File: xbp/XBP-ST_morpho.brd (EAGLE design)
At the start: 68.9 x 31.1 mm, 4 parts

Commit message: XBX ST morpho Adapter version 1.0
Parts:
- removed JP6: VCCDin, pinhead:1X01
- added JP1: (no value), pinhead:2X10
- JP3: value (none) -> VCCDin; device pinhead:2X10 -> pinhead:1X01
- moved JP3 14.4 mm to (14.0, 5.08), turned to 0 degrees
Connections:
- net GND: now also JP1.19, JP1.20, JP1.8, JP4.20; no longer JP3.8
- net N$6: now also JP1.16, JP2.4, JP3.1; no longer JP3.16, JP6.1
- net RSTD: now also JP1.14; no longer JP3.14
- net VCCD: now also JP1.5; no longer JP3.5
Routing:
- net N$6: track 13.5 -> 34.0 mm
- net TF0D: track 43.3 -> 34.3 mm, vias 0 -> 1
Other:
- board text added: "Align with Top of ST Morpho Connector (pins 1 and 2)"
- board text added: "JP1"
- board text added: "JP3"
- board text added: "JP4"
- board text added: "VCCDin"
- board text added: "VIN"
- board text added: "XXBX: XBP - ST morpho Adapter"
- board text added: "rev 1.0"
- board text removed: "+"
- board text removed: "0"
- board text removed: "0b"
- board text removed: "1"
- board text removed: "10"
- board text removed: "100"
- board text removed: "11"
- board text removed: "1a"
- board text removed: "1b"
- board text removed: "2"
- board text removed: "20"
- board text removed: "200"
- board text removed: "21"
- board text removed: "25"
- board text removed: "2a"
- board text removed: "2b"
- board text removed: "3"
- board text removed: "30"
- board text removed: "31"
- board text removed: "3a"
- board text removed: "3b"
- board text removed: "40"
- board text removed: "50"
- board text removed: "5V"
- board text removed: "Activity"
- board text removed: "C1"
- board text removed: "C2"
- board text removed: "C3"
- board text removed: "GS0a"
- board text removed: "GS1a"
- board text removed: "GS2a"
- board text removed: "GS3a"
- board text removed: "GS3b"
- board text removed: "Gain"
- board text removed: "IC1"
- board text removed: "J1"
- board text removed: "J2"
- board text removed: "J3"
- board text removed: "J4"
- board text removed: "JP5"
- board text removed: "PWR3"
- board text removed: "Power"
- board text removed: "Q1"
- board text removed: "Q2"
- board text removed: "Q3"
- board text removed: "Q4"
- board text removed: "Q5"
- board text removed: "Q6"
- board text removed: "Q7"
- board text removed: "Q8"
- board text removed: "R1"
- board text removed: "R10"
- board text removed: "R11"
- board text removed: "R12"
- board text removed: "R13"
- board text removed: "R2"
- board text removed: "R3"
- board text removed: "R4"
- board text removed: "R5"
- board text removed: "R6"
- board text removed: "R7"
- board text removed: "R8"
- board text removed: "R9"
- board text removed: "RST0"
- board text removed: "RST1"
- board text removed: "SJ1"
- board text removed: "SJ2"
- board text removed: "SJ3"
- board text removed: "SJ4"
- board text removed: "SJ5"
- board text removed: "TF0"
- board text removed: "TF1"
- board text removed: "TF2"
- board text removed: "TF3"
- board text removed: "U1"
- board text removed: "VccD"
- board text removed: "VccH"
- board text removed: "VccP"
- board text removed: "X1"
- board text removed: "XBH"
- board text removed: "XBP"
- board text removed: "rev 2.0"

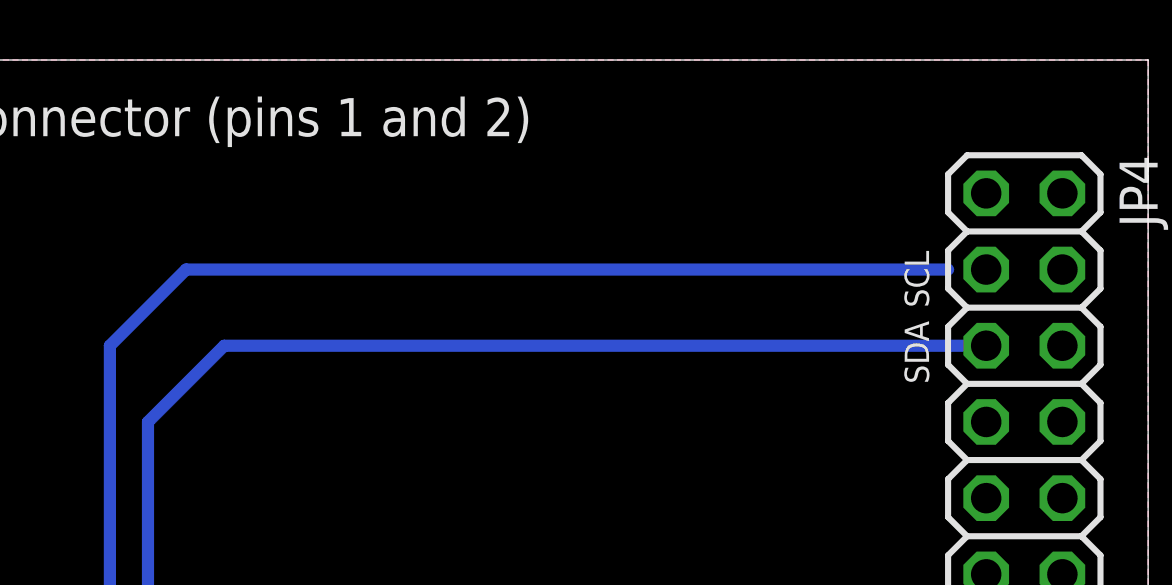
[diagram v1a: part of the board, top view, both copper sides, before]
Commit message: SCL was not connected to ST Morpho Pin
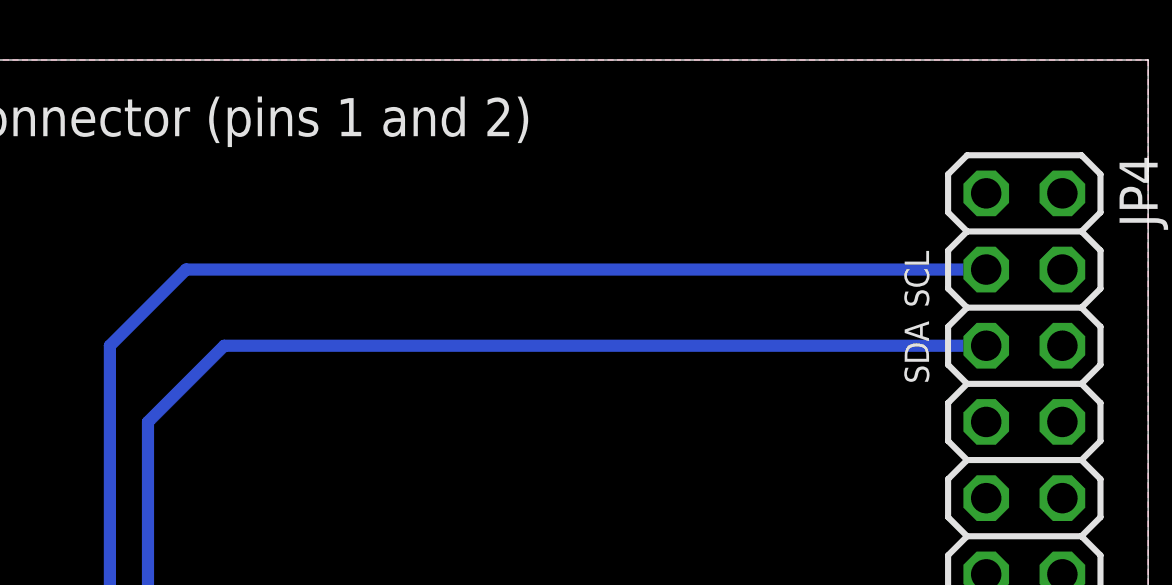
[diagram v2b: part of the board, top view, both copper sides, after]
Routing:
- net SCLD: track 46.0 -> 47.3 mm
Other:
- board text added: "rev 1.1"
- board text removed: "rev 1.0"
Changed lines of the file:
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@@
 <text x="34.29" y="24.13" size="1.27" layer="122" font="vector" ratio="16" rot="MR0" align="bottom-center">cryptography.gmu.edu</text>
 <text x="34.29" y="21.59" size="1.27" layer="122" font="vector" ratio="16" rot="MR0" align="bottom-center">XXBX: XBP - ST morpho Adapter</text>
-<text x="34.29" y="19.05" size="1.27" layer="122" font="vector" ratio="16" rot="MR0" align="bottom-center">rev 1.0</text>
+<text x="34.29" y="19.05" size="1.27" layer="122" font="vector" ratio="16" rot="MR0" align="bottom-center">rev 1.1</text>
 <text x="6.35" y="28.575" size="1.27" layer="121" font="vector" ratio="16">Align with Top of ST Morpho Connector (pins 1 and 2)</text>
 </plain>
@@
 <wire x1="34.29" y1="6.35" x2="34.29" y2="21.59" width="0.4064" layer="16"/>
 <wire x1="34.29" y1="21.59" x2="36.83" y2="24.13" width="0.4064" layer="16"/>
-<wire x1="36.83" y1="24.13" x2="62.23" y2="24.13" width="0.4064" layer="16"/>
-<wire x1="62.23" y1="24.13" x2="63.5" y2="24.13" width="0" layer="19" extent="16-16"/>
+<wire x1="36.83" y1="24.13" x2="63.5" y2="24.13" width="0.4064" layer="16"/>
 </signal>
 <signal name="SDAD">
